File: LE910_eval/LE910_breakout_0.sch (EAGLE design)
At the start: 2 parts, among them M1 LE910_V2_BREAKOUT_CASEDGES, U1 LE910_V2

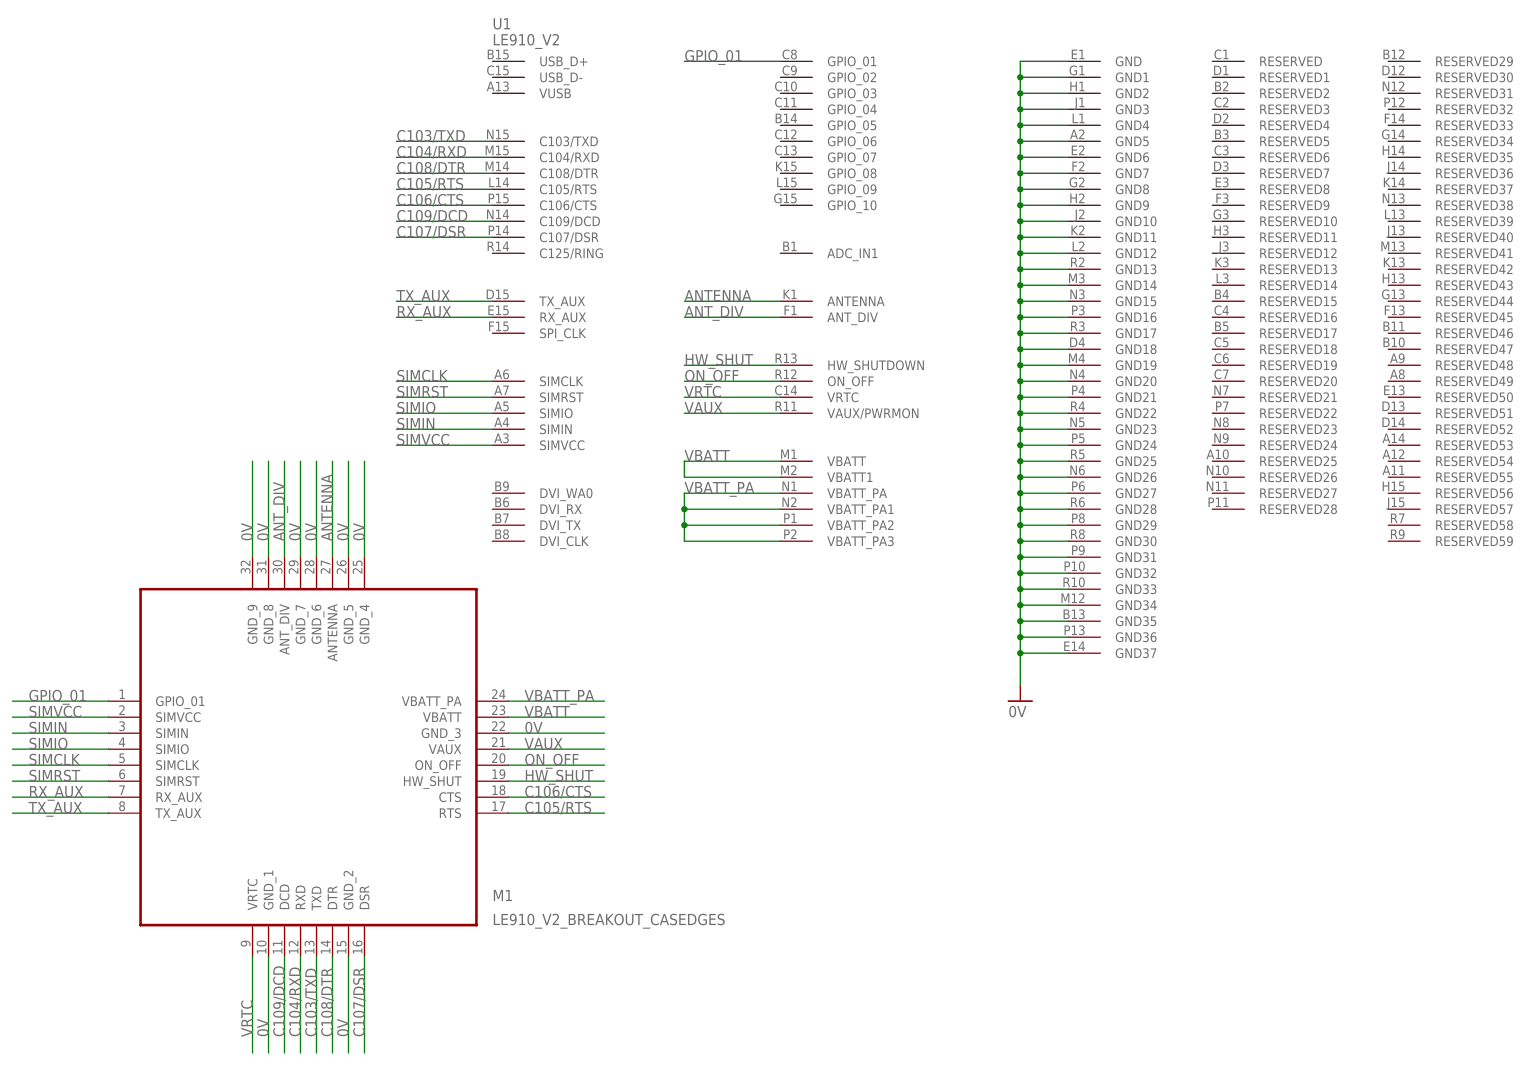
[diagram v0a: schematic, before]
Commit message: デザイン修正
・ブレークアウト基板のピンレイアウトを修正
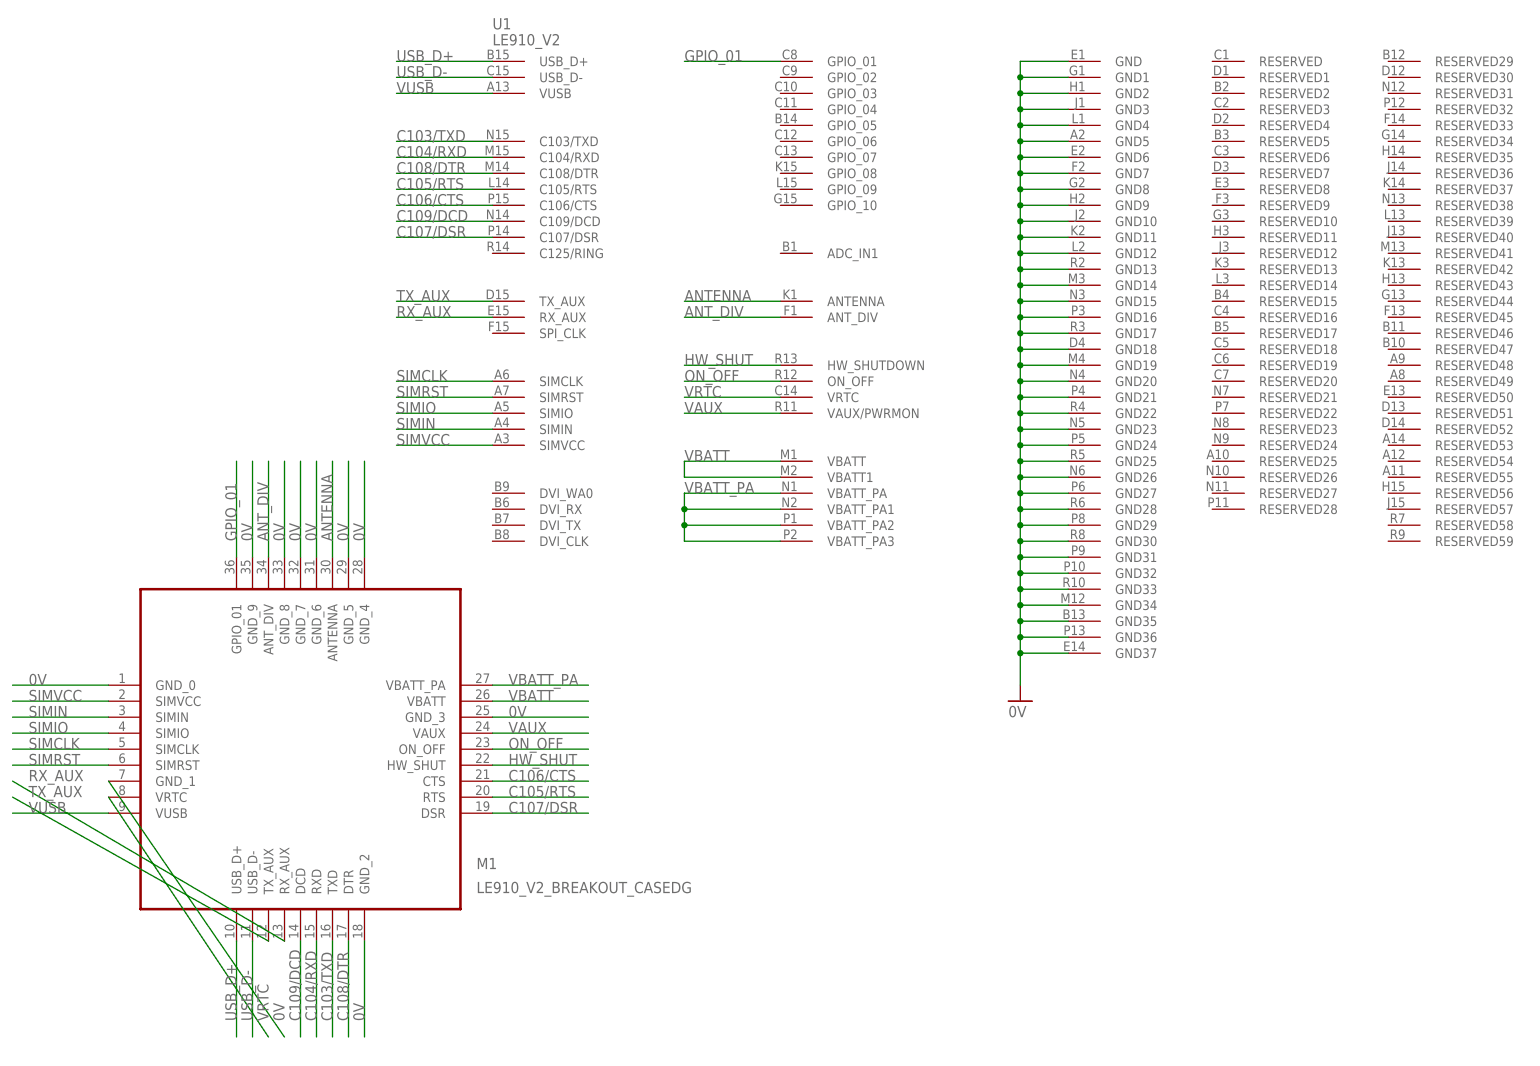
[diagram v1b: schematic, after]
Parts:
- M1: value LE910_V2_BREAKOUT_CASEDGES -> LE910_V2_BREAKOUT_CASEDG; device Modules:LE910_V2_BREAKOUT_CASEDGES -> Modules:LE910_V2_BREAKOUT_CASEDG
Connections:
- new net USB_D+: M1.USB_D+, U1.USB_D+
- new net USB_D-: M1.USB_D-, U1.USB_D-
- new net VUSB: M1.VUSB, U1.VUSB
- net 0V: now also M1.GND_0
